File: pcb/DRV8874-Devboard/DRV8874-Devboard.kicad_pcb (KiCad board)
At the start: 4 copper layers, 65 x 67 mm, 51 parts, among them J1 Conn_01x04_Pin, J10 Conn_01x06_Pin, J12 Conn_01x03_Pin, J2 Screw_Terminal_01x02, J3 Conn_01x03_Pin, J4 Conn_01x03_Pin, J5 Conn_01x04_Pin, J6 Conn_01x03_Pin, J7 Conn_01x03_Pin, J9 Conn_01x03_Pin, U1 DRV8874, U2 BL9342, U3 DRV8874, U4 SN65HVD230, U5 TPS16630PWPR, U7 TinyThinker_J1

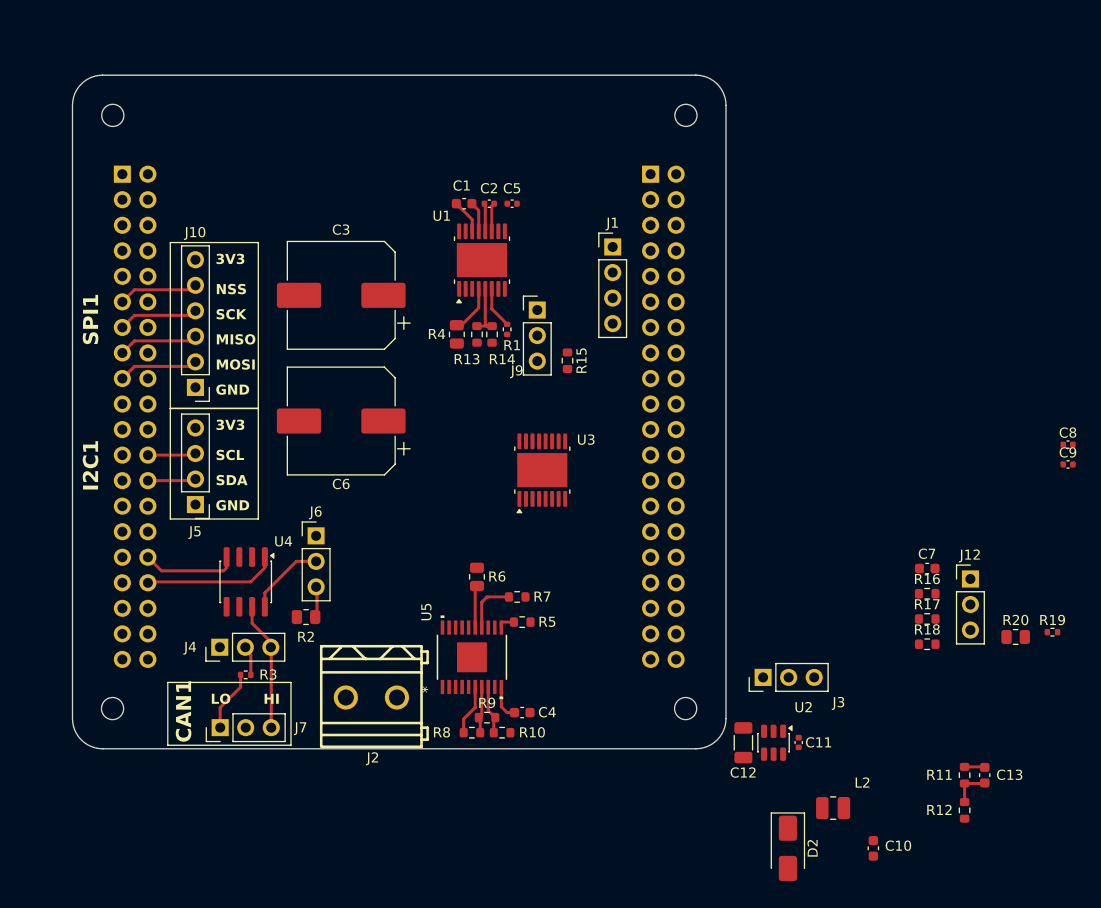
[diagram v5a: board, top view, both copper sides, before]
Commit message: Routed and laid out BL9342 step down
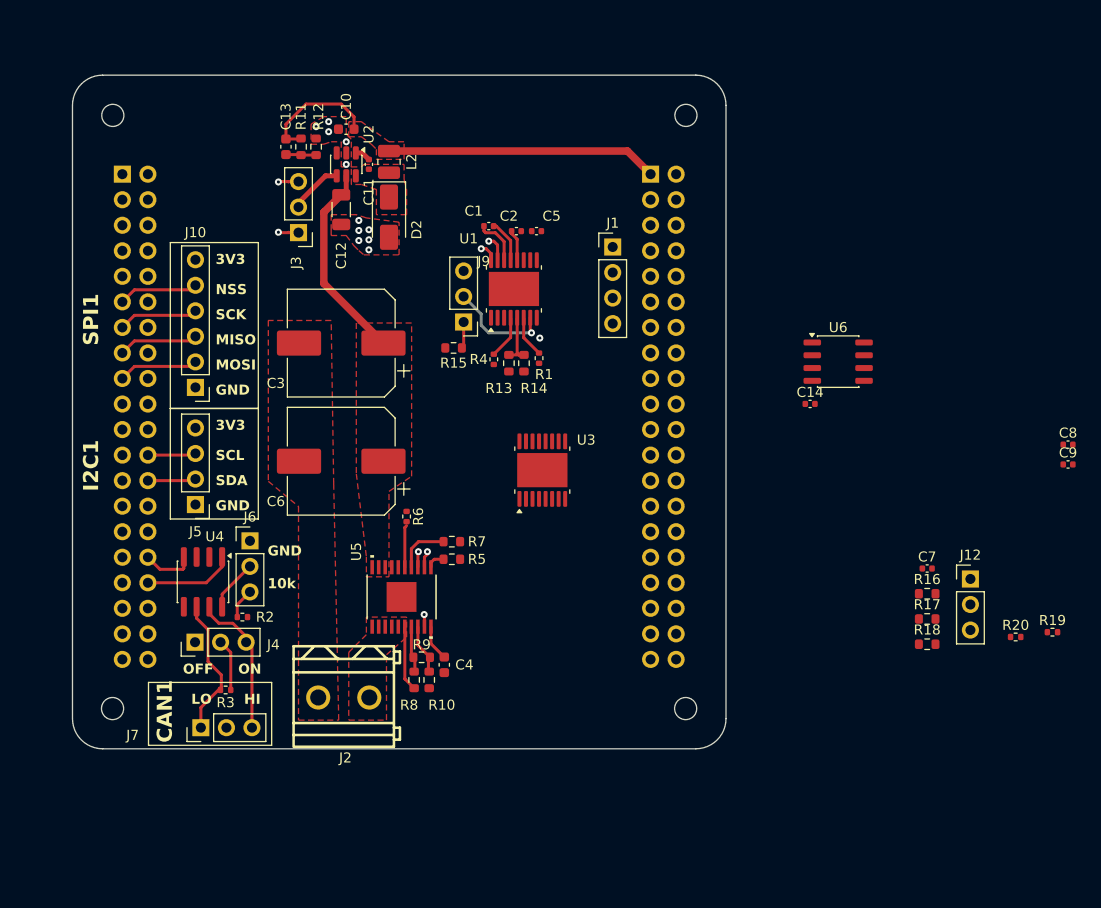
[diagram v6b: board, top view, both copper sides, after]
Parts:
- added C14: 100nF, Capacitor_SMD:C_0402_1005Metric, F.Cu at (170.1, 72.3)
- added U6: M95320-WMN6TP, Package_SO:SO-8_3.9x4.9mm_P1.27mm, F.Cu at (172.9, 68.1)
- C1, C7: footprint Capacitor_SMD:C_0603_1608Metric -> Capacitor_SMD:C_0402_1005Metric
- R2, R20, R4, R6: footprint Resistor_SMD:R_0805_2012Metric -> Resistor_SMD:R_0402_1005Metric
- moved C13 93.5 mm to (118.0, 46.7)
- moved R12 92.3 mm to (121.0, 46.7), turned to -90 degrees
- moved R11 90.9 mm to (119.5, 46.7)
- moved C10 88.7 mm to (124.0, 45.0), turned to 180 degrees
- moved L2 78.0 mm to (128.2, 48.2), turned to 90 degrees
- moved D2 74.3 mm to (128.2, 53.7)
- moved C11 71.7 mm to (126.2, 48.5)
- moved U2 71.5 mm to (124.0, 48.5)
- moved C12 66.4 mm to (123.5, 53.0)
- moved J3 64.0 mm to (119.2, 55.3), turned to 180 degrees
- moved R15 11.4 mm to (134.7, 66.7), turned to 180 degrees
- moved R5 9.38 mm to (134.5, 87.8)
- moved R6 9.22 mm to (130.0, 83.5)
- moved U5 9.22 mm to (129.5, 91.5)
- moved C4 9.09 mm to (133.8, 98.2), turned to -90 degrees
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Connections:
- U7 pad 71: unconnected-(U7B-SPI2_MOSI-Pad71) -> /SPI2_MOSI
- U7 pad 73: unconnected-(U7B-SPI2_MISO-Pad73) -> /SPI2_MISO
- U7 pad 75: unconnected-(U7B-SPI2_SCK-Pad75) -> /SPI2_SCK
- U7 pad 77: unconnected-(U7B-SPI2_NSS-Pad77) -> /SPI2_NSS
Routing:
- net +5V: track 2.02 -> 39.3 mm
- net +BATT_PROT: track 2.85 -> 19.8 mm
- net /A_IMODE: track 0.00 -> 10.5 mm, vias 0 -> 1
- net /CAN_L: track 6.09 -> 13.9 mm
- net GND: track 0.00 -> 7.44 mm, vias 0 -> 16
- net +3.3V: track 0.00 -> 5.42 mm, vias 0 -> 3
- net /BL_EN: track 0.00 -> 5.34 mm
- net /CAN1_RX: track 9.59 -> 5.24 mm
- net /CAN1_TX: track 13.3 -> 9.15 mm
- net /A_IMODE_R: track 0.00 -> 2.65 mm
- net /CAN_RS: track 7.77 -> 5.16 mm
- net /CAN_TERM: track 2.73 -> 5.17 mm
- net /CAN_H: track 12.3 -> 14.6 mm
- net /BL_BST: track 0.00 -> 1.57 mm
- net +BATT_RAW: track 5.02 -> 6.51 mm
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- added copper zone on F.Cu, net +5V
- added copper zone on F.Cu, net +BATT_PROT
- added copper zone on F.Cu, net +BATT_RAW
- added copper zone on F.Cu, net /BL_SW
- added copper zone on F.Cu, net GND
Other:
- board text added: "10k"
- board text added: "OFF"
- board text added: "ON"

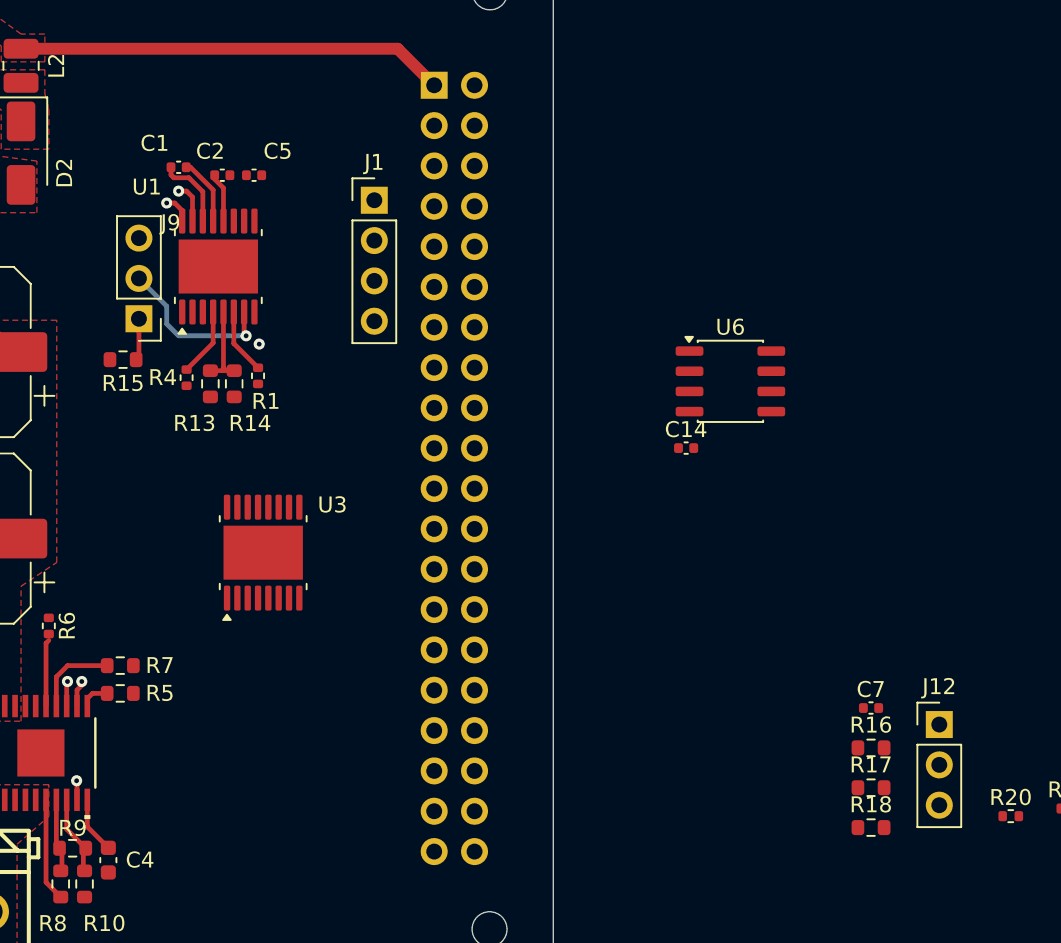
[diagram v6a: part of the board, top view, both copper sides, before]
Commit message: starting routing EEPROM
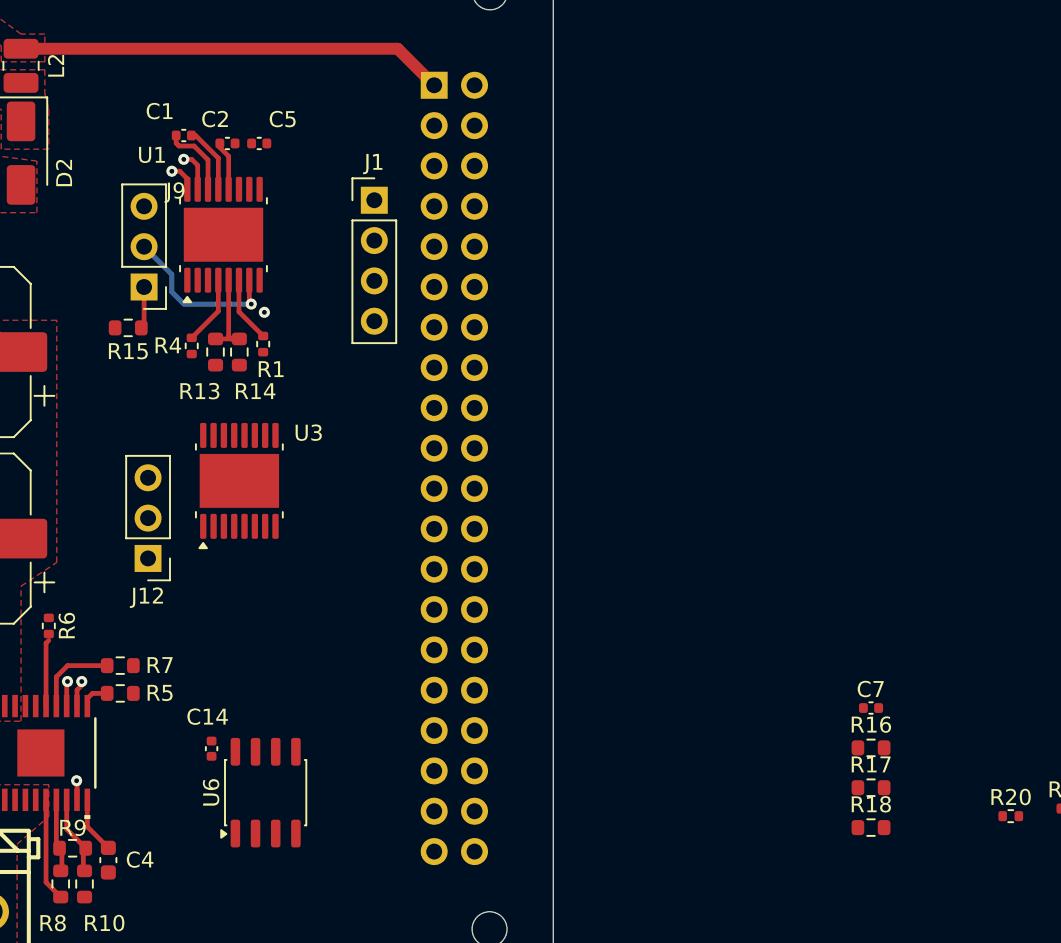
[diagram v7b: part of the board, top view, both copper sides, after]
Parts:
- moved J12 50.9 mm to (136.2, 79.2), turned to 180 degrees
- moved U6 39.1 mm to (143.7, 94.0), turned to 90 degrees
- moved C14 35.4 mm to (140.2, 91.2), turned to -90 degrees
- moved U3 4.76 mm to (142.0, 74.4)
- moved C1 2.03 mm to (138.5, 52.6)
- moved C2 2.03 mm to (141.2, 53.1)
- moved C5 2.03 mm to (143.2, 53.1)
- moved J9 2.03 mm to (136.0, 62.2)
- moved R1 2.03 mm to (143.5, 65.8)
- moved R13 2.03 mm to (140.5, 66.2)
- moved R14 2.03 mm to (142.0, 66.2)
- moved R15 2.03 mm to (135.0, 64.7)
- moved R4 2.03 mm to (139.0, 65.9)
- moved U1 2.03 mm to (141.0, 58.9)

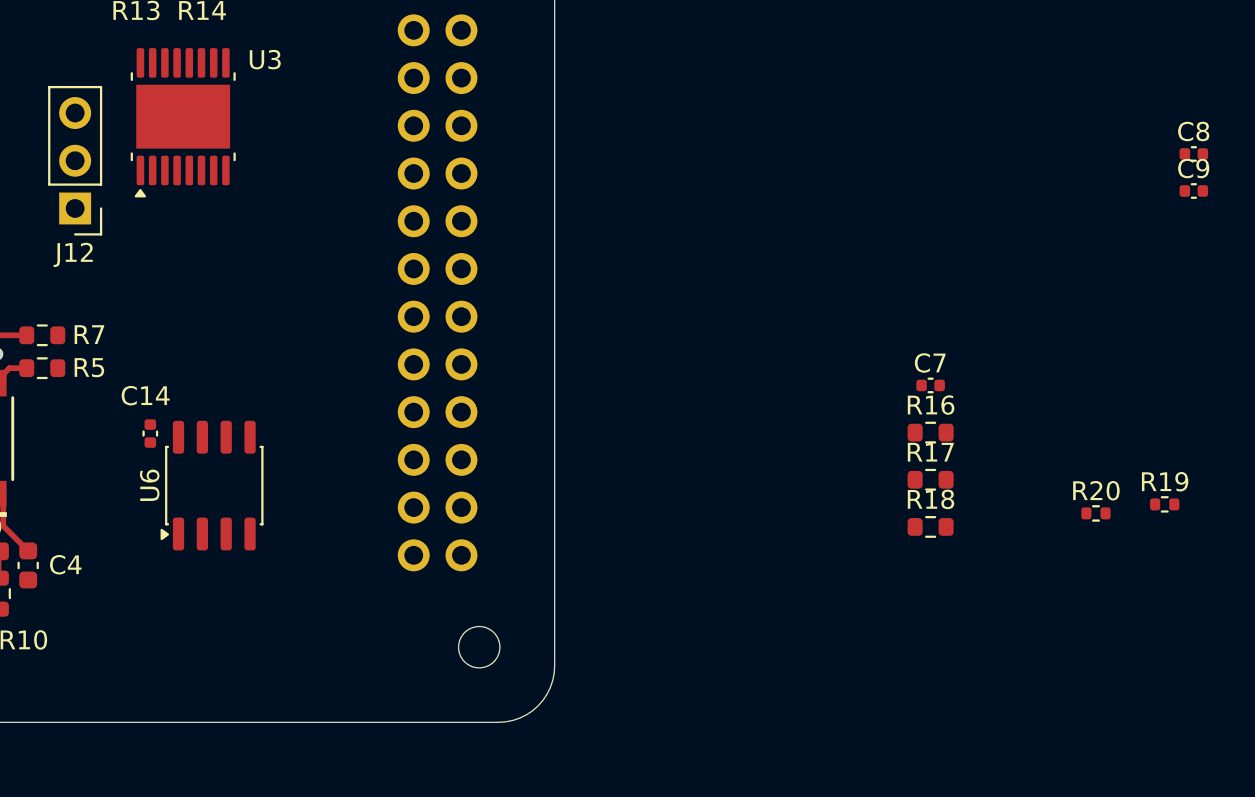
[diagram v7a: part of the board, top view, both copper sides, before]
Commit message: generated CSV to see pricing
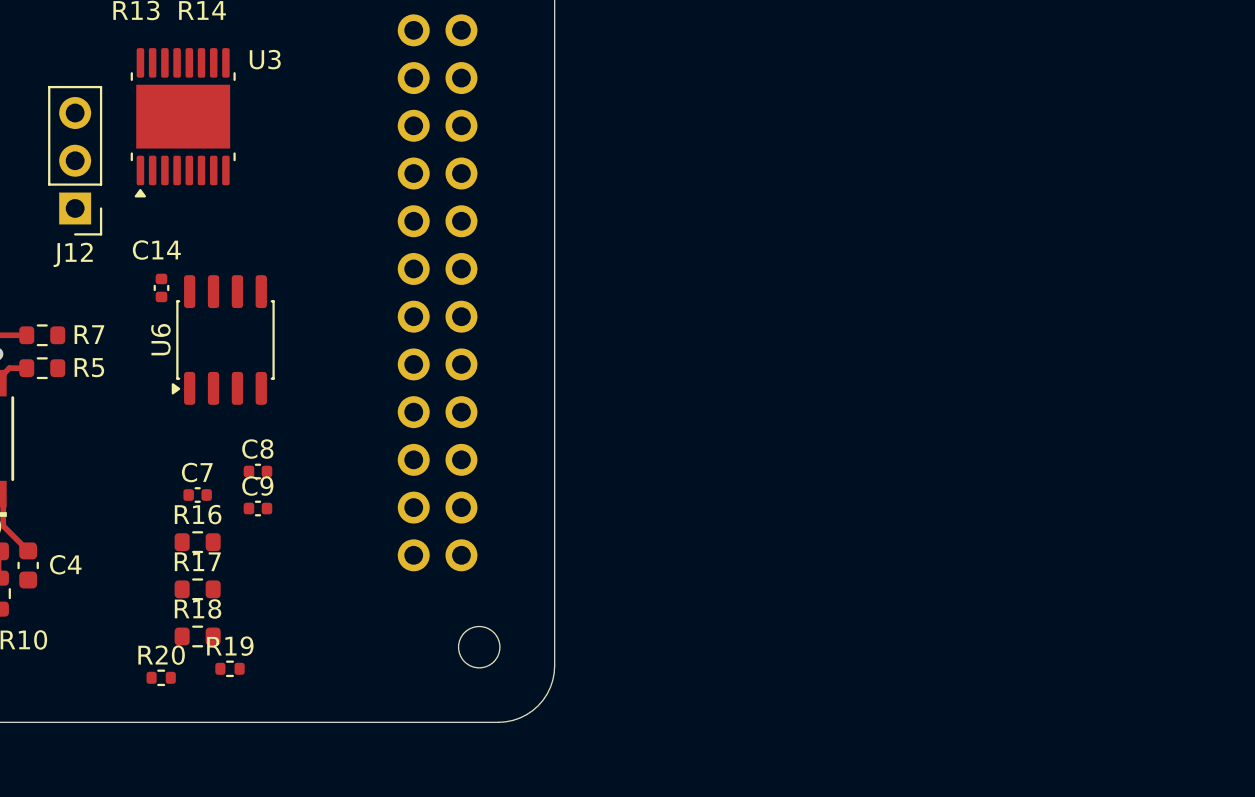
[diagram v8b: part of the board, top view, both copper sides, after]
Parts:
- moved C8 52.6 mm to (146.0, 93.2)
- moved C9 52.6 mm to (146.0, 95.2)
- moved R19 50.5 mm to (144.5, 103.8)
- moved R20 50.5 mm to (140.8, 104.2)
- moved C7 39.4 mm to (142.8, 94.5)
- moved R16 39.4 mm to (142.8, 97.0)
- moved R17 39.4 mm to (142.8, 99.5)
- moved R18 39.4 mm to (142.8, 102.0)
- moved C14 7.77 mm to (140.8, 83.5)
- moved U6 7.77 mm to (144.2, 86.2)
